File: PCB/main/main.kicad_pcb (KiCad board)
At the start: 2 copper layers, 55 x 85.5 mm, 70 parts, among them J1 Conn_01x06_Pin, J2 Headlight, J3 Conn_01x05_Pin, J4 Conn_01x03_Pin, J5 Battery, Q1 NPN, Q2 NPN, U1 ESP32-WROOM-32, U2 TB6612FNG, U3 TB6612FNG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

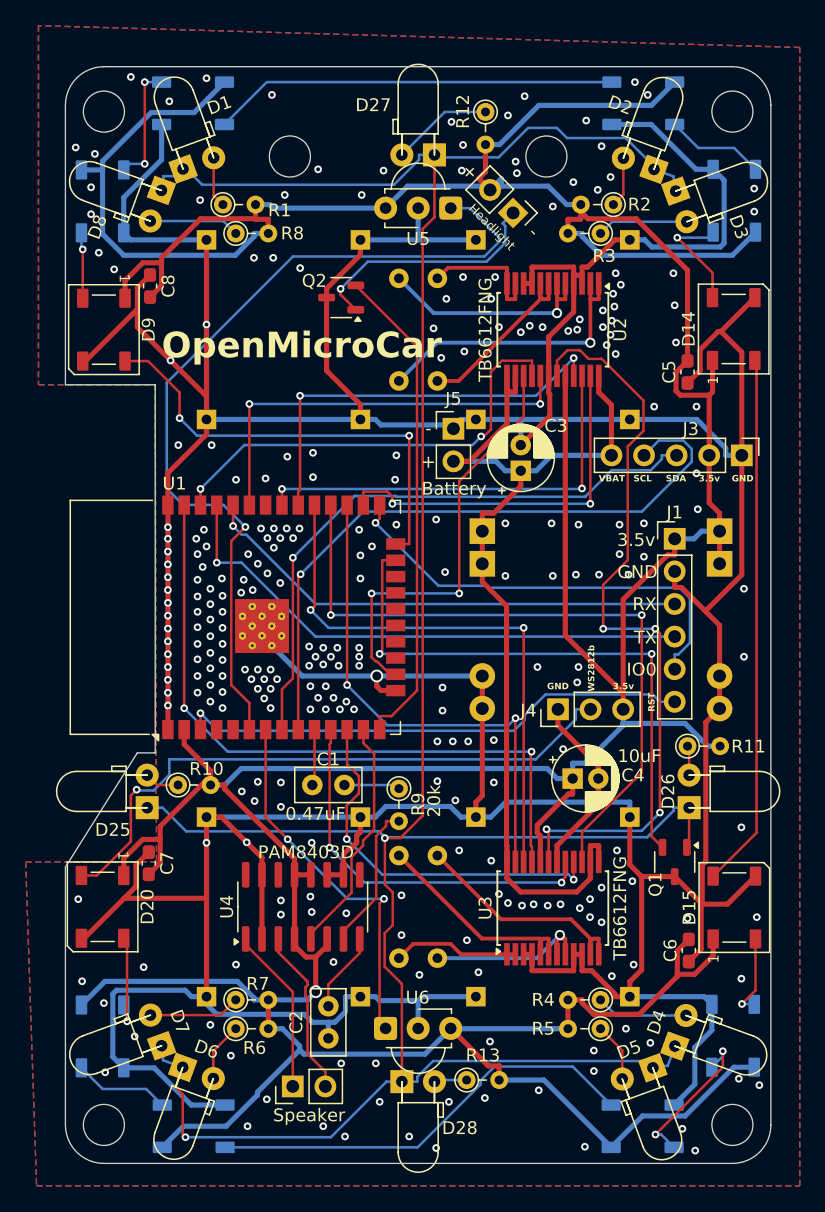
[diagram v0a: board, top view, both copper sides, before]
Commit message: Base Resistors and README.md
Added base resistors to the headlight and IR led transistors (facepalm), and added to the main README.md.
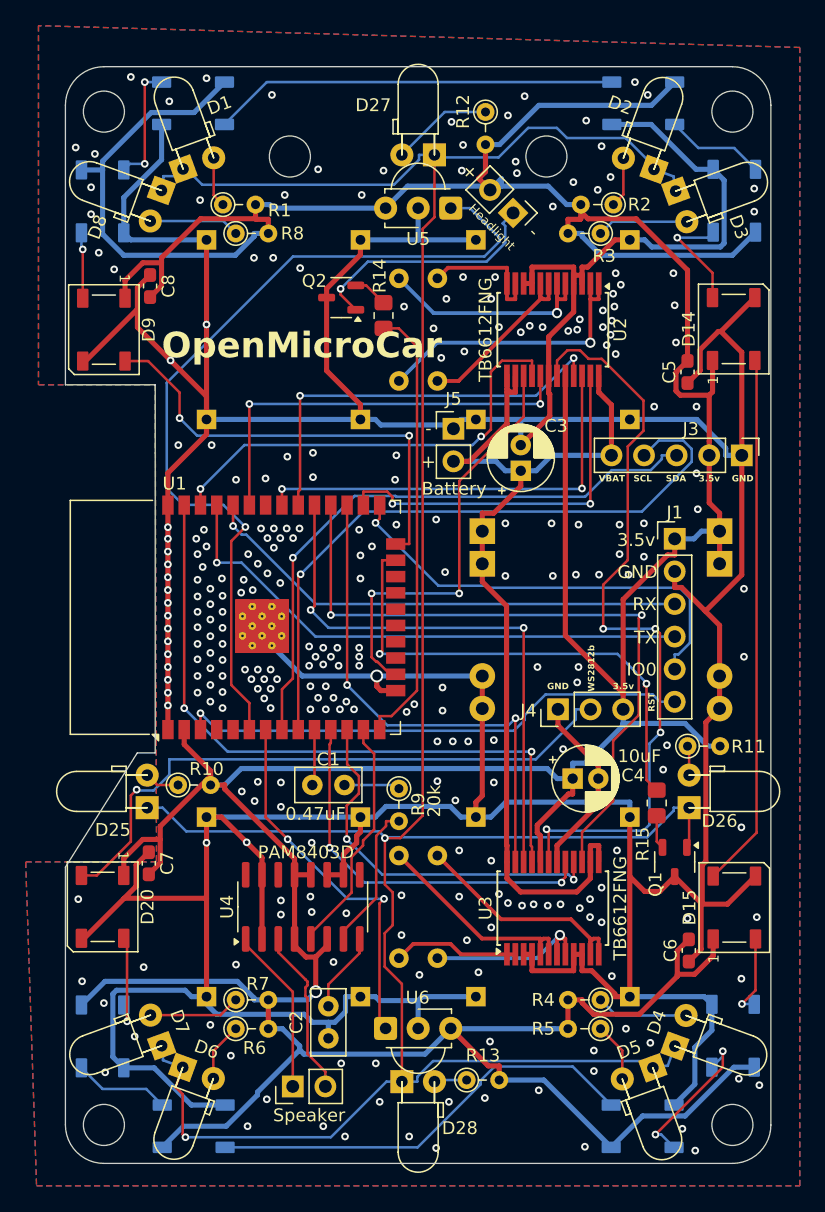
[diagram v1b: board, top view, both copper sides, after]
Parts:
- added R14: 100, Resistor_SMD:R_0805_2012Metric_Pad1.20x1.40mm_HandSolder, F.Cu at (139.8, 73.9)
- added R15: 100, Resistor_SMD:R_0805_2012Metric_Pad1.20x1.40mm_HandSolder, F.Cu at (161.1, 111.9)
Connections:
- Q1 pad 2: IR Out -> Net-(Q1-B)
- Q2 pad 2: Headlight_Control -> Net-(Q2-B)
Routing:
- net IR Out: track 45.1 -> 39.1 mm
- net Headlight_Control: track 38.4 -> 34.8 mm
- net Net-(Q2-B): track 0.00 -> 2.72 mm
- net Net-(Q1-B): track 0.00 -> 2.65 mm
- net GND: track 522.4 -> 523.5 mm, vias 272 -> 277
